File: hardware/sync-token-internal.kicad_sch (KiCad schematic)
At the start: 4 parts, among them U1 74AHC74, U2 74LVC2G125

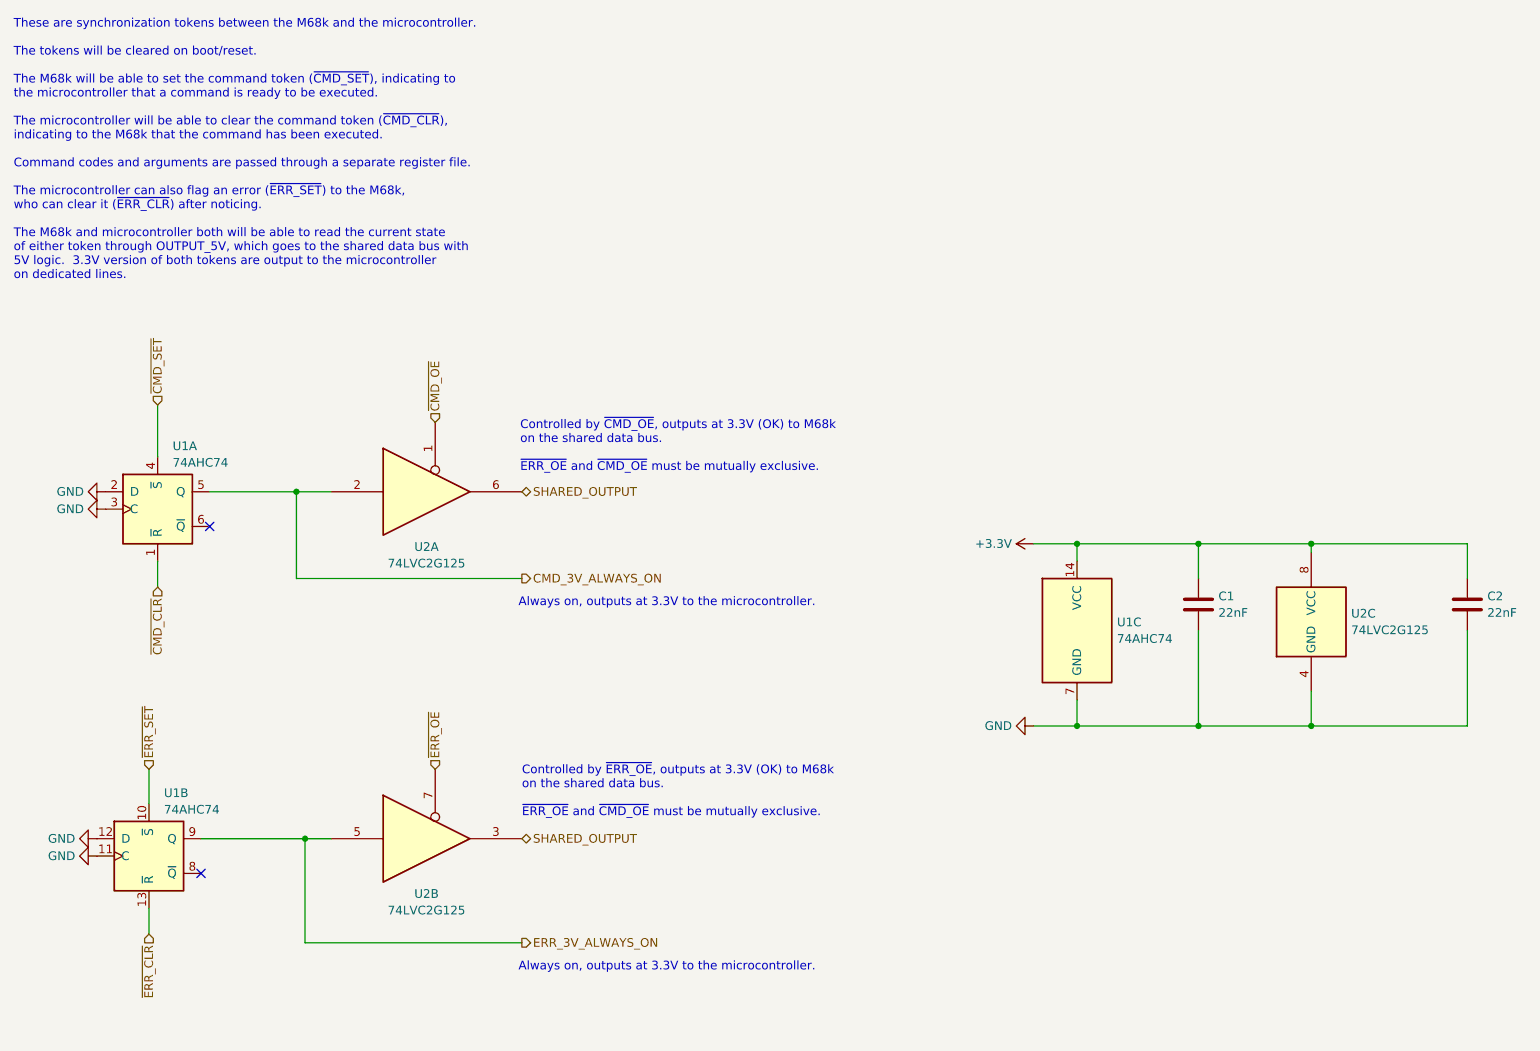
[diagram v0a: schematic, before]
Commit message: Reannotate schematics and drop debug bridges
Parts are now numbered starting at 0 for cart, 100 for SRAM, 300 for
microcontroller.

Also, drop debug bridges that made routing more difficult and had the
same names across prototype boards.

Hopefully this will help avoid naming conflicts for the unified PCB.

Also, redo prototype PCB layouts.

Now that all the names have changed, update board layouts.
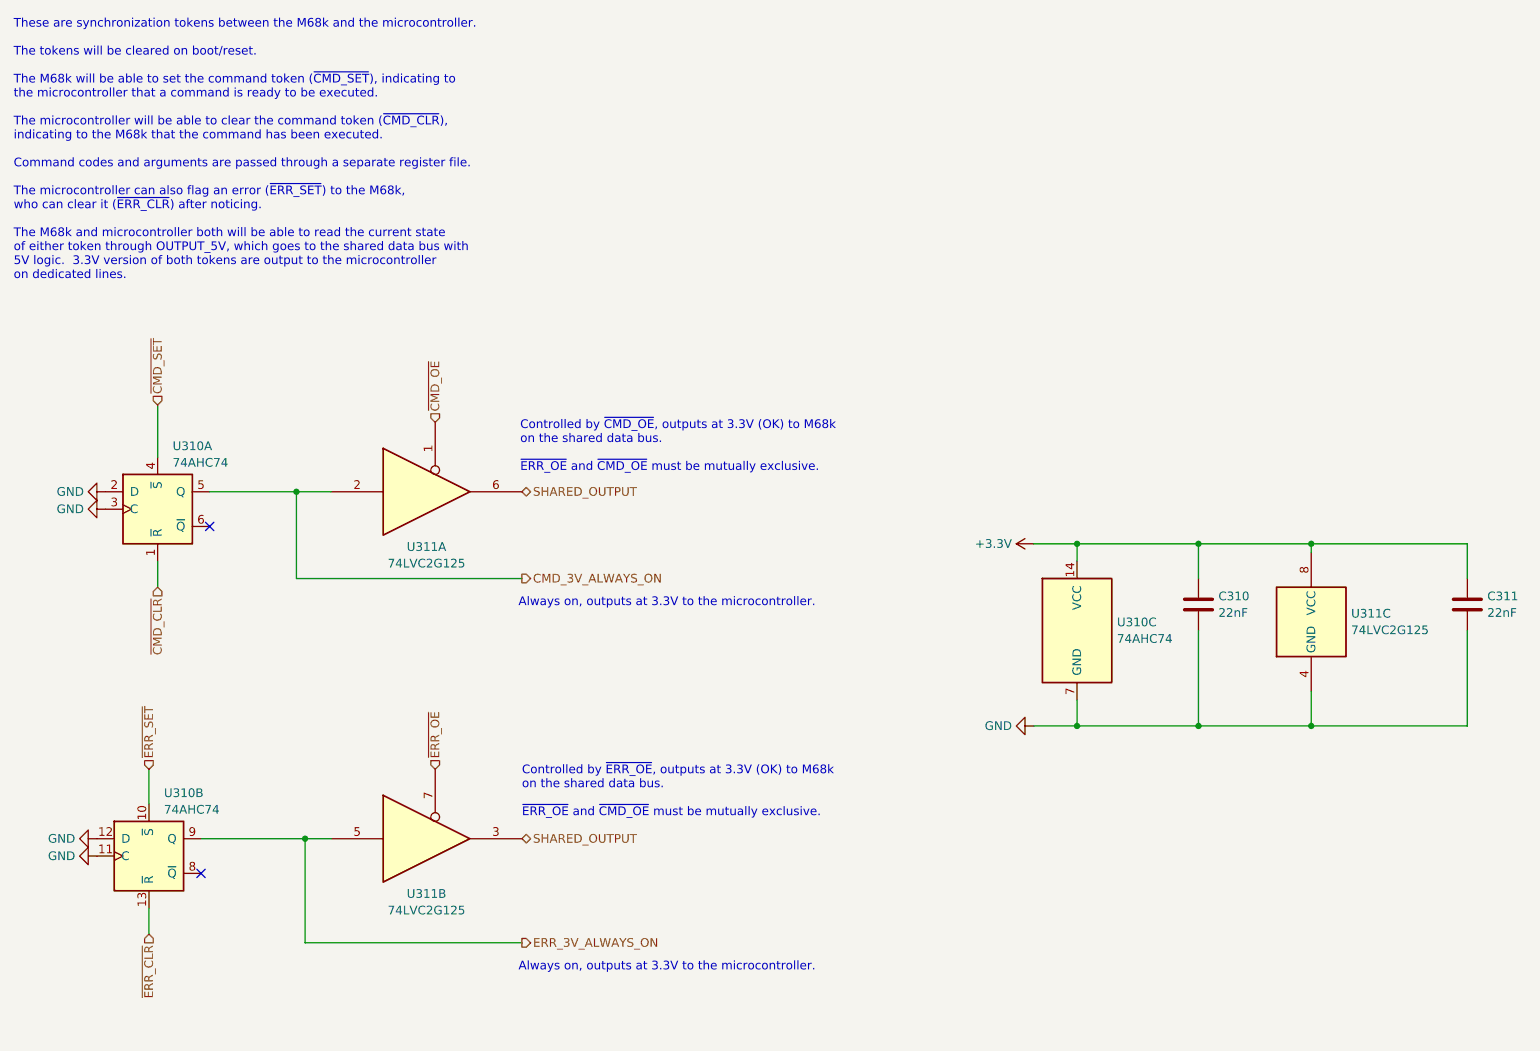
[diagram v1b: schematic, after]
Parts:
- renumbered C1 to C310, C2 to C311, U1 to U310, U2 to U311
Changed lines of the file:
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@@
 		(dnp no)
 		(fields_autoplaced yes)
-		(property "Reference" "U2"
+		(property "Reference" "U311"
 			(at 92.71 99.5101 0)
 			(effects
@@
 		(instances
 			(project "microcontroller"
+				(path "/686046a3-64dc-4761-a4ce-3e2fd65204d5/7e8ae288-5866-48d7-b597-b9928e48743f/2d231838-6b64-4e52-8f19-d0e449327717"
+					(reference "U311")
+					(unit 1)
+				)
+			)
+			(project "microcontroller"
 				(path "/eb0e957f-b2ea-4261-97c1-e28148a3f6e1/1f234c04-2a4a-4cc4-8cff-97e40dff5b3b/2d231838-6b64-4e52-8f19-d0e449327717"
-					(reference "U2")
+					(reference "U307")
 					(unit 1)
 				)
@@
 		(dnp no)
 		(fields_autoplaced yes)
-		(property "Reference" "U2"
+		(property "Reference" "U311"
 			(at 92.71 150.3101 0)
 			(effects
@@
 		(instances
 			(project "microcontroller"
+				(path "/686046a3-64dc-4761-a4ce-3e2fd65204d5/7e8ae288-5866-48d7-b597-b9928e48743f/2d231838-6b64-4e52-8f19-d0e449327717"
+					(reference "U311")
+					(unit 2)
+				)
+			)
+			(project "microcontroller"
 				(path "/eb0e957f-b2ea-4261-97c1-e28148a3f6e1/1f234c04-2a4a-4cc4-8cff-97e40dff5b3b/2d231838-6b64-4e52-8f19-d0e449327717"
-					(reference "U2")
+					(reference "U307")
 					(unit 2)
 				)
@@
 		(on_board yes)
 		(dnp no)
-		(property "Reference" "#PWR012"
+		(property "Reference" "#PWR0353"
 			(at 38.1 144.78 0)
 			(effects
@@
 		(instances
 			(project "microcontroller"
+				(path "/686046a3-64dc-4761-a4ce-3e2fd65204d5/7e8ae288-5866-48d7-b597-b9928e48743f/2d231838-6b64-4e52-8f19-d0e449327717"
+					(reference "#PWR0353")
+					(unit 1)
+				)
+			)
+			(project "microcontroller"
 				(path "/eb0e957f-b2ea-4261-97c1-e28148a3f6e1/1f234c04-2a4a-4cc4-8cff-97e40dff5b3b/2d231838-6b64-4e52-8f19-d0e449327717"
-					(reference "#PWR012")
+					(reference "#PWR0353")
 					(unit 1)
 				)
@@
 		(dnp no)
 		(fields_autoplaced yes)
-		(property "Reference" "C1"
+		(property "Reference" "C310"
 			(at 208.661 106.7378 0)
 			(effects
@@
 		(instances
 			(project "microcontroller"
+				(path "/686046a3-64dc-4761-a4ce-3e2fd65204d5/7e8ae288-5866-48d7-b597-b9928e48743f/2d231838-6b64-4e52-8f19-d0e449327717"
+					(reference "C310")
+					(unit 1)
+				)
+			)
+			(project "microcontroller"
 				(path "/eb0e957f-b2ea-4261-97c1-e28148a3f6e1/1f234c04-2a4a-4cc4-8cff-97e40dff5b3b/2d231838-6b64-4e52-8f19-d0e449327717"
-					(reference "C1")
+					(reference "C306")
 					(unit 1)
 				)
@@
 		(dnp no)
 		(fields_autoplaced yes)
-		(property "Reference" "U2"
+		(property "Reference" "U311"
 			(at 228.092 109.2778 0)
 			(effects
@@
 		(instances
 			(project "microcontroller"
+				(path "/686046a3-64dc-4761-a4ce-3e2fd65204d5/7e8ae288-5866-48d7-b597-b9928e48743f/2d231838-6b64-4e52-8f19-d0e449327717"
+					(reference "U311")
+					(unit 3)
+				)
+			)
+			(project "microcontroller"
 				(path "/eb0e957f-b2ea-4261-97c1-e28148a3f6e1/1f234c04-2a4a-4cc4-8cff-97e40dff5b3b/2d231838-6b64-4e52-8f19-d0e449327717"
-					(reference "U2")
+					(reference "U307")
 					(unit 3)
 				)
@@
 		(dnp no)
 		(fields_autoplaced yes)
-		(property "Reference" "U1"
+		(property "Reference" "U310"
 			(at 54.2641 135.5555 0)
 			(effects
@@
 		(instances
 			(project "microcontroller"
+				(path "/686046a3-64dc-4761-a4ce-3e2fd65204d5/7e8ae288-5866-48d7-b597-b9928e48743f/2d231838-6b64-4e52-8f19-d0e449327717"
+					(reference "U310")
+					(unit 2)
+				)
+			)
+			(project "microcontroller"
 				(path "/eb0e957f-b2ea-4261-97c1-e28148a3f6e1/1f234c04-2a4a-4cc4-8cff-97e40dff5b3b/2d231838-6b64-4e52-8f19-d0e449327717"
-					(reference "U1")
+					(reference "U306")
 					(unit 2)
 				)
@@
 		(dnp no)
 		(fields_autoplaced yes)
-		(property "Reference" "#PWR016"
+		(property "Reference" "#PWR0357"
 			(at 175.26 125.73 0)
 			(effects
@@
 		(instances
 			(project "microcontroller"
+				(path "/686046a3-64dc-4761-a4ce-3e2fd65204d5/7e8ae288-5866-48d7-b597-b9928e48743f/2d231838-6b64-4e52-8f19-d0e449327717"
+					(reference "#PWR0357")
+					(unit 1)
+				)
+			)
+			(project "microcontroller"
 				(path "/eb0e957f-b2ea-4261-97c1-e28148a3f6e1/1f234c04-2a4a-4cc4-8cff-97e40dff5b3b/2d231838-6b64-4e52-8f19-d0e449327717"
-					(reference "#PWR016")
+					(reference "#PWR0357")
 					(unit 1)
 				)
@@
 		(dnp no)
 		(fields_autoplaced yes)
-		(property "Reference" "U1"
+		(property "Reference" "U310"
 			(at 193.802 110.5478 0)
 			(effects
@@
 		(instances
 			(project "microcontroller"
+				(path "/686046a3-64dc-4761-a4ce-3e2fd65204d5/7e8ae288-5866-48d7-b597-b9928e48743f/2d231838-6b64-4e52-8f19-d0e449327717"
+					(reference "U310")
+					(unit 3)
+				)
+			)
+			(project "microcontroller"
 				(path "/eb0e957f-b2ea-4261-97c1-e28148a3f6e1/1f234c04-2a4a-4cc4-8cff-97e40dff5b3b/2d231838-6b64-4e52-8f19-d0e449327717"
-					(reference "U1")
+					(reference "U306")
 					(unit 3)
 				)
@@
 		(dnp no)
 		(fields_autoplaced yes)
-		(property "Reference" "C2"
+		(property "Reference" "C311"
 			(at 248.031 106.7378 0)
 			(effects
@@
 		(instances
 			(project "microcontroller"
+				(path "/686046a3-64dc-4761-a4ce-3e2fd65204d5/7e8ae288-5866-48d7-b597-b9928e48743f/2d231838-6b64-4e52-8f19-d0e449327717"
+					(reference "C311")
+					(unit 1)
+				)
+			)
+			(project "microcontroller"
 				(path "/eb0e957f-b2ea-4261-97c1-e28148a3f6e1/1f234c04-2a4a-4cc4-8cff-97e40dff5b3b/2d231838-6b64-4e52-8f19-d0e449327717"
-					(reference "C2")
+					(reference "C307")
 					(unit 1)
 				)
@@
 		(dnp no)
 		(fields_autoplaced yes)
-		(property "Reference" "U1"
+		(property "Reference" "U310"
 			(at 55.5341 84.7555 0)
 			(effects
@@
 		(instances
 			(project "microcontroller"
+				(path "/686046a3-64dc-4761-a4ce-3e2fd65204d5/7e8ae288-5866-48d7-b597-b9928e48743f/2d231838-6b64-4e52-8f19-d0e449327717"
+					(reference "U310")
+					(unit 1)
+				)
+			)
+			(project "microcontroller"
 				(path "/eb0e957f-b2ea-4261-97c1-e28148a3f6e1/1f234c04-2a4a-4cc4-8cff-97e40dff5b3b/2d231838-6b64-4e52-8f19-d0e449327717"
-					(reference "U1")
+					(reference "U306")
 					(unit 1)
 				)
@@
 		(on_board yes)
 		(dnp no)
-		(property "Reference" "#PWR03"
+		(property "Reference" "#PWR0352"
 			(at 38.1 142.24 0)
 			(effects
@@
 		(instances
 			(project "microcontroller"
+				(path "/686046a3-64dc-4761-a4ce-3e2fd65204d5/7e8ae288-5866-48d7-b597-b9928e48743f/2d231838-6b64-4e52-8f19-d0e449327717"
+					(reference "#PWR0352")
+					(unit 1)
+				)
+			)
+			(project "microcontroller"
 				(path "/eb0e957f-b2ea-4261-97c1-e28148a3f6e1/1f234c04-2a4a-4cc4-8cff-97e40dff5b3b/2d231838-6b64-4e52-8f19-d0e449327717"
-					(reference "#PWR03")
+					(reference "#PWR0352")
 					(unit 1)
 				)
@@
 		(dnp no)
 		(fields_autoplaced yes)
-		(property "Reference" "#PWR013"
+		(property "Reference" "#PWR0354"
 			(at 39.37 91.44 0)
 			(effects
@@
 		(instances
 			(project "microcontroller"
+				(path "/686046a3-64dc-4761-a4ce-3e2fd65204d5/7e8ae288-5866-48d7-b597-b9928e48743f/2d231838-6b64-4e52-8f19-d0e449327717"
+					(reference "#PWR0354")
+					(unit 1)
+				)
+			)
+			(project "microcontroller"
 				(path "/eb0e957f-b2ea-4261-97c1-e28148a3f6e1/1f234c04-2a4a-4cc4-8cff-97e40dff5b3b/2d231838-6b64-4e52-8f19-d0e449327717"
-					(reference "#PWR013")
+					(reference "#PWR0354")
 					(unit 1)
 				)
@@
 		(dnp no)
 		(fields_autoplaced yes)
-		(property "Reference" "#PWR014"
+		(property "Reference" "#PWR0355"
 			(at 39.37 93.98 0)
 			(effects
@@
 		(instances
 			(project "microcontroller"
+				(path "/686046a3-64dc-4761-a4ce-3e2fd65204d5/7e8ae288-5866-48d7-b597-b9928e48743f/2d231838-6b64-4e52-8f19-d0e449327717"
+					(reference "#PWR0355")
+					(unit 1)
+				)
+			)
+			(project "microcontroller"
 				(path "/eb0e957f-b2ea-4261-97c1-e28148a3f6e1/1f234c04-2a4a-4cc4-8cff-97e40dff5b3b/2d231838-6b64-4e52-8f19-d0e449327717"
-					(reference "#PWR014")
+					(reference "#PWR0355")
 					(unit 1)
 				)
@@
 		(dnp no)
 		(fields_autoplaced yes)
-		(property "Reference" "#PWR015"
+		(property "Reference" "#PWR0356"
 			(at 185.42 99.06 0)
 			(effects
@@
 		(instances
 			(project "microcontroller"
+				(path "/686046a3-64dc-4761-a4ce-3e2fd65204d5/7e8ae288-5866-48d7-b597-b9928e48743f/2d231838-6b64-4e52-8f19-d0e449327717"
+					(reference "#PWR0356")
+					(unit 1)
+				)
+			)
+			(project "microcontroller"
 				(path "/eb0e957f-b2ea-4261-97c1-e28148a3f6e1/1f234c04-2a4a-4cc4-8cff-97e40dff5b3b/2d231838-6b64-4e52-8f19-d0e449327717"
-					(reference "#PWR015")
-					(unit 1)
-				)
+					(reference "#PWR0356")
+					(unit 1)
+				)
